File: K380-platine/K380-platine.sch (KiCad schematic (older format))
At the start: 33 parts, among them J1 JST-PH 2, J2 Conn_01x23, J3 MicroMod-M.2E, J4 USB_C_Receptacle_USB2.0, Q1 PMost Enc FET -20V, Q2 Q_NMOS_DGS, SW1 EG1215AA, SW2 SW_Push, SW3 SW_Push, U1 XC6220B331MR, U2 MCP73831-2-OT

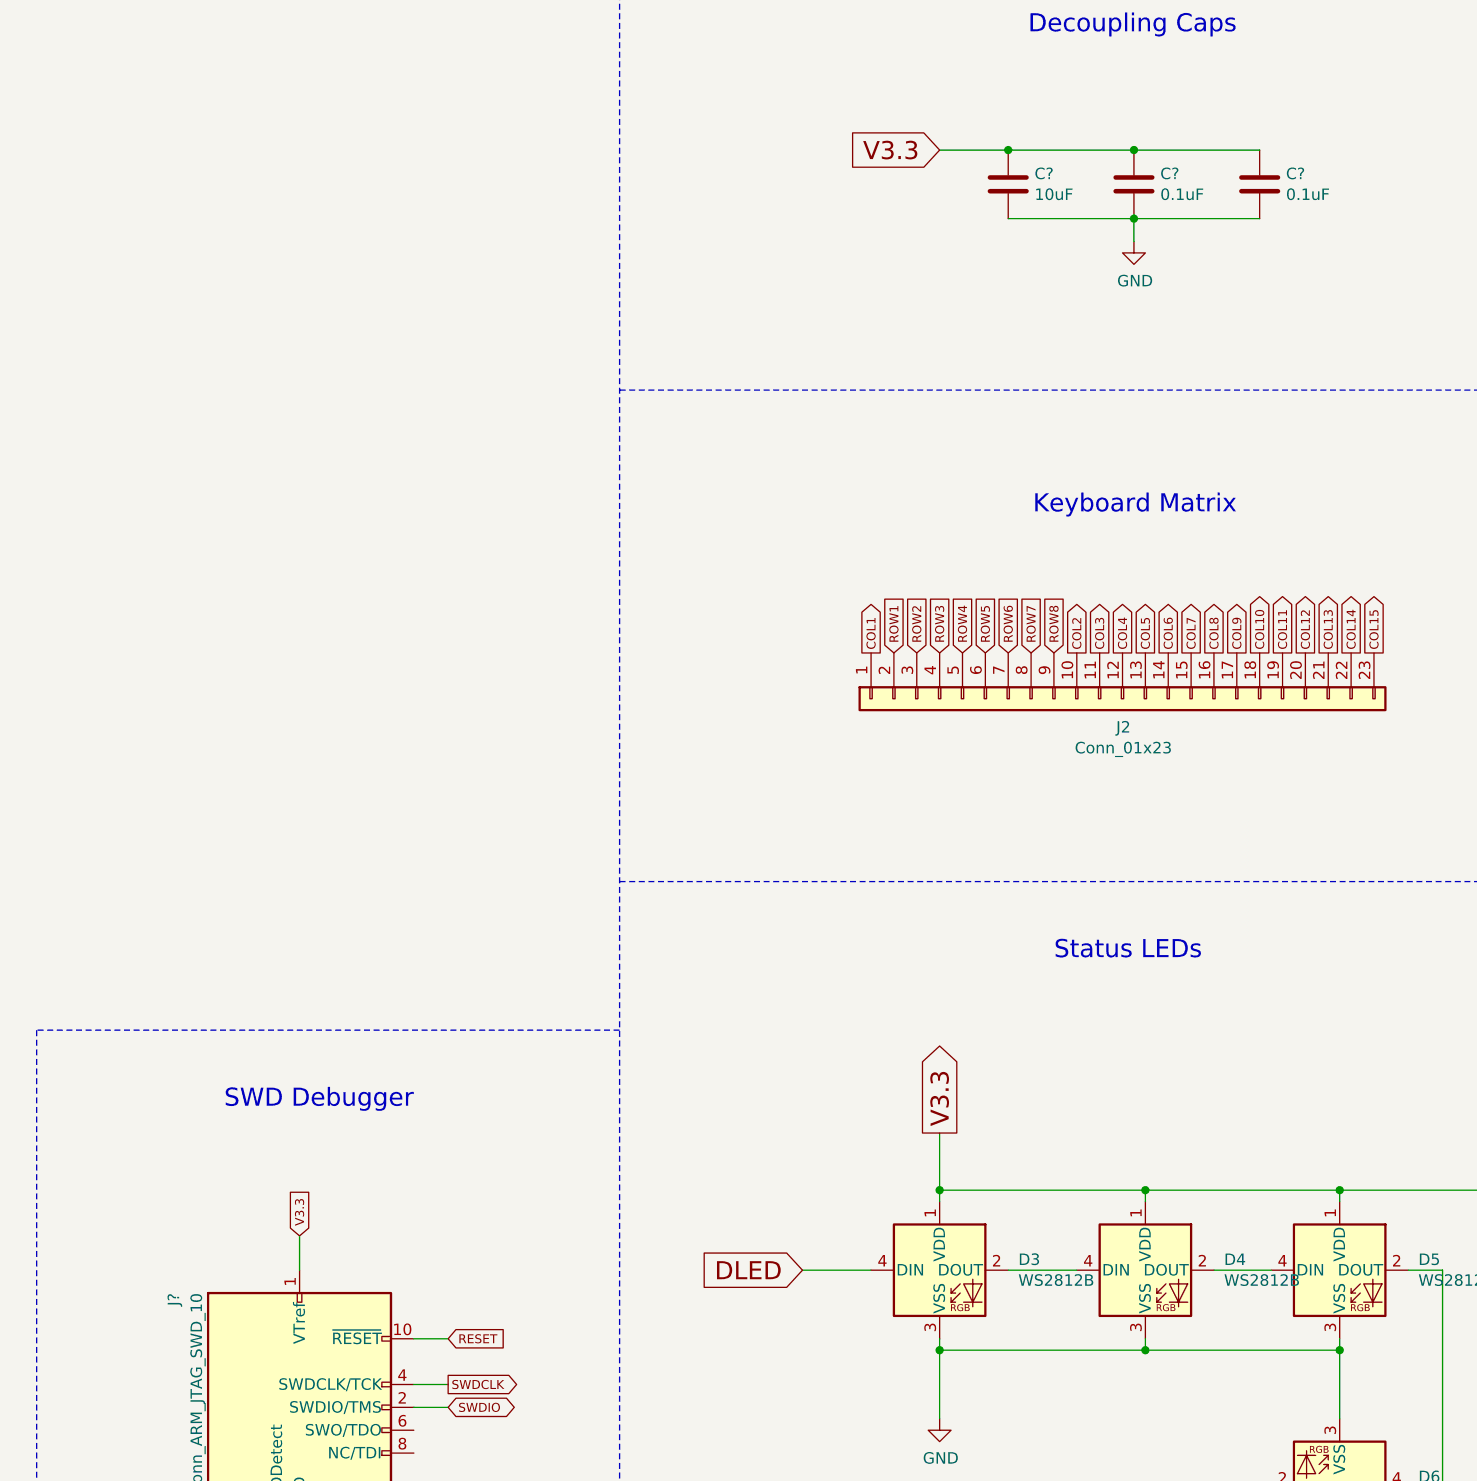
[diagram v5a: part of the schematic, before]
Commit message: Assigned footprint to all components
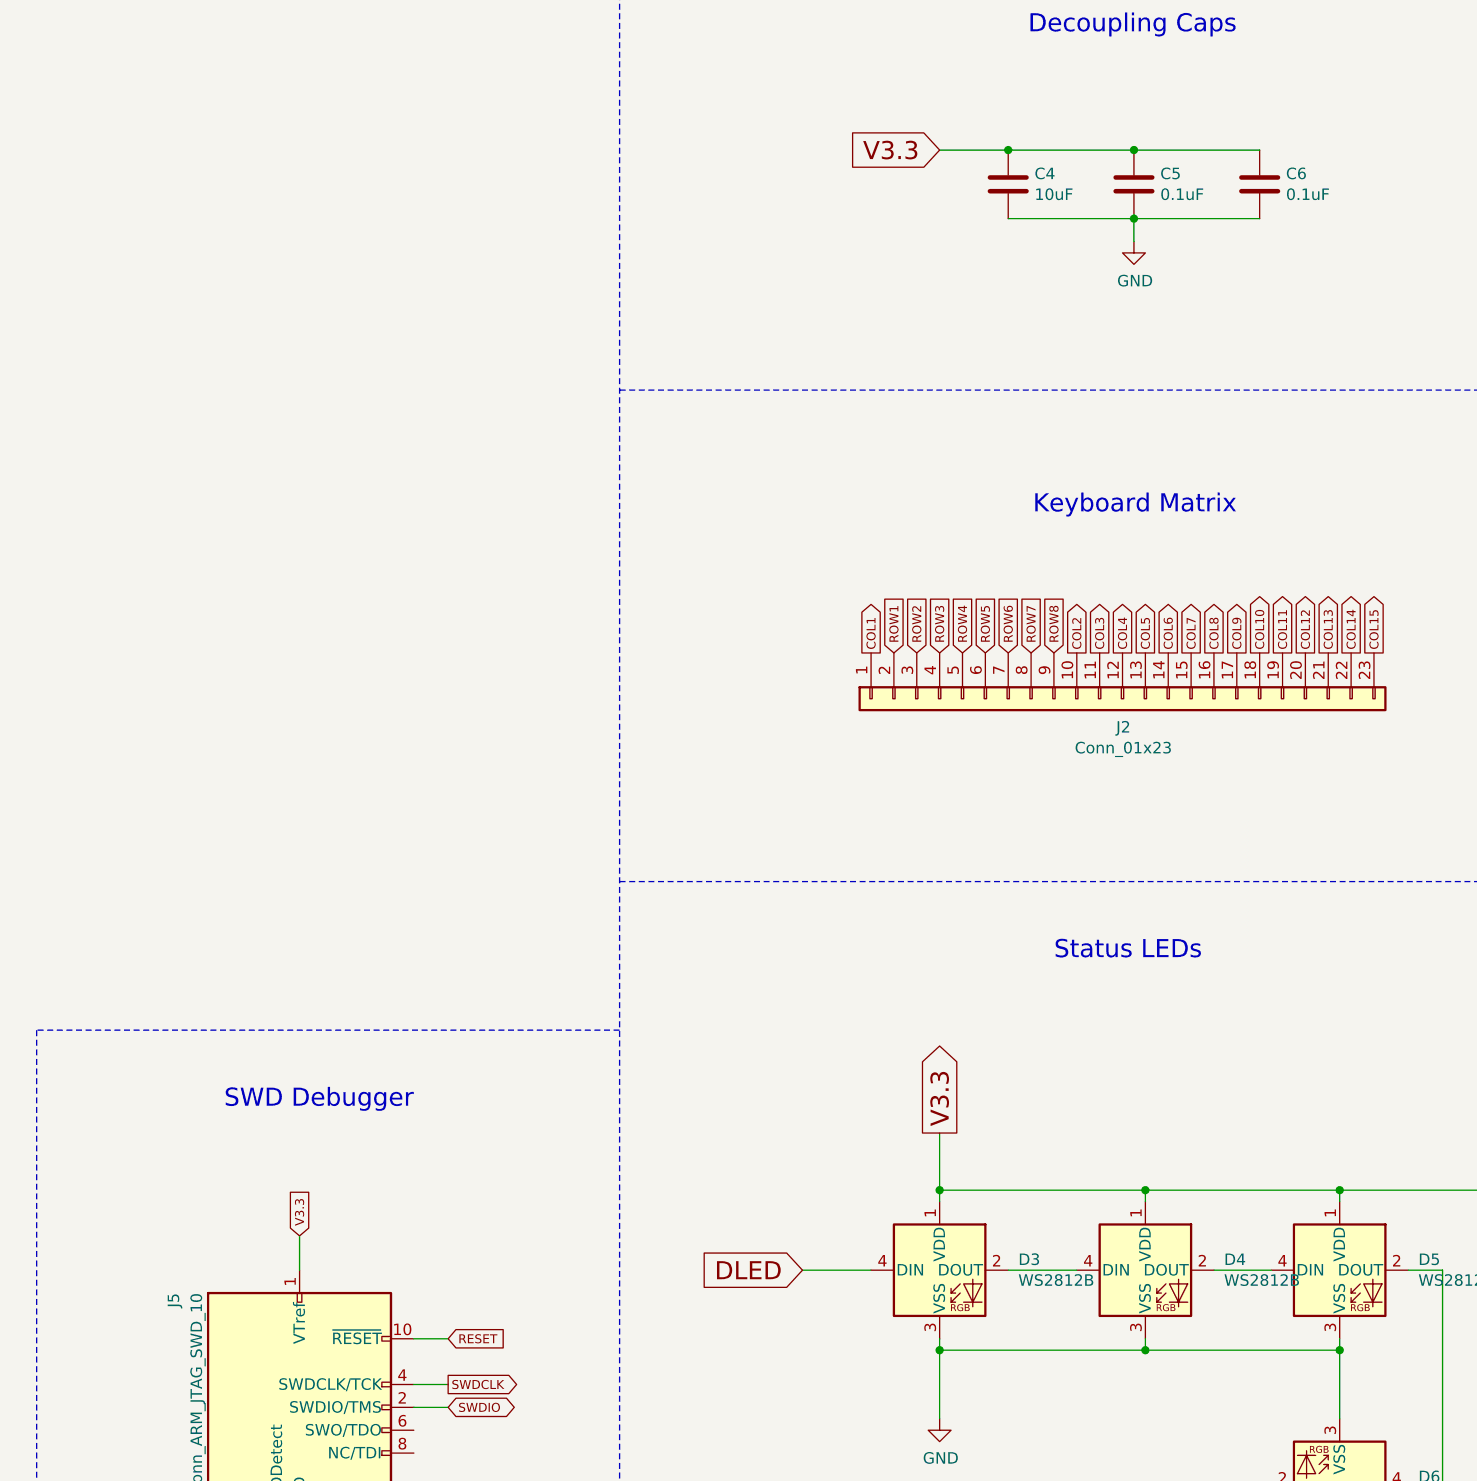
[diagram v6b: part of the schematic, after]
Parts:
- C1, C2, C3: footprint (none) -> Capacitor_SMD:C_1206_3216Metric_Pad1.33x1.80mm_HandSolder
- C4, C5, C6: renamed from C?; footprint (none) -> Capacitor_SMD:C_1206_3216Metric_Pad1.33x1.80mm_HandSolder
- D2: footprint (none) -> Diode_SMD:D_SMA_Handsoldering
- J4, R1, R2, R3, R4, R5, R6, R7, R8, R9: footprint (none) -> Resistor_SMD:R_1206_3216Metric_Pad1.30x1.75mm_HandSolder
- J5: renamed from J?; footprint (none) -> Connector_PinHeader_1.27mm:PinHeader_2x05_P1.27mm_Vertical_SMD
- Q2: footprint (none) -> Package_TO_SOT_SMD:SOT-23
- SW2, SW3: footprint (none) -> LibraryLoader:MJTP1140AAUTR
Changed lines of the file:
@@
 F 0 "C1" H 1742 10446 50  0000 L CNN
 F 1 "10uF" H 1742 10355 50  0000 L CNN
-F 2 "" H 1650 10400 50  0001 C CNN
+F 2 "Capacitor_SMD:C_1206_3216Metric_Pad1.33x1.80mm_HandSolder" H 1650 10400 50  0001 C CNN
 F 3 "~" H 1650 10400 50  0001 C CNN
 	1    1650 10400
@@
 F 0 "R1" H 1209 10446 50  0000 L CNN
 F 1 "100K" H 1209 10355 50  0000 L CNN
-F 2 "" H 1150 10400 50  0001 C CNN
+F 2 "Resistor_SMD:R_1206_3216Metric_Pad1.30x1.75mm_HandSolder" H 1150 10400 50  0001 C CNN
 F 3 "~" H 1150 10400 50  0001 C CNN
 	1    1150 10400
@@
 F 0 "R2" V 1904 10250 50  0000 C CNN
 F 1 "100K" V 1995 10250 50  0000 C CNN
-F 2 "" H 2100 10250 50  0001 C CNN
+F 2 "Resistor_SMD:R_1206_3216Metric_Pad1.30x1.75mm_HandSolder" H 2100 10250 50  0001 C CNN
 F 3 "~" H 2100 10250 50  0001 C CNN
 	1    2100 10250
@@
 F 0 "C2" H 3492 10446 50  0000 L CNN
 F 1 "4.7uF" H 3492 10355 50  0000 L CNN
-F 2 "" H 3400 10400 50  0001 C CNN
+F 2 "Capacitor_SMD:C_1206_3216Metric_Pad1.33x1.80mm_HandSolder" H 3400 10400 50  0001 C CNN
 F 3 "~" H 3400 10400 50  0001 C CNN
 	1    3400 10400
@@
 F 0 "R3" H 5609 9996 50  0000 L CNN
 F 1 "RProg" H 5609 9905 50  0000 L CNN
-F 2 "" H 5550 9950 50  0001 C CNN
+F 2 "Resistor_SMD:R_1206_3216Metric_Pad1.30x1.75mm_HandSolder" H 5550 9950 50  0001 C CNN
 F 3 "~" H 5550 9950 50  0001 C CNN
 	1    5550 9950
@@
 F 0 "C3" H 6992 9896 50  0000 L CNN
 F 1 "10uF" H 6992 9805 50  0000 L CNN
-F 2 "" H 6900 9850 50  0001 C CNN
+F 2 "Capacitor_SMD:C_1206_3216Metric_Pad1.33x1.80mm_HandSolder" H 6900 9850 50  0001 C CNN
 F 3 "~" H 6900 9850 50  0001 C CNN
 	1    6900 9850
@@
 F 0 "J4" H 8757 10617 50  0000 C CNN
 F 1 "USB_C_Receptacle_USB2.0" H 8757 10526 50  0000 C CNN
-F 2 "" H 8800 9750 50  0001 C CNN
+F 2 "Resistor_SMD:R_1206_3216Metric_Pad1.30x1.75mm_HandSolder" H 8800 9750 50  0001 C CNN
 F 3 "https://www.usb.org/sites/default/files/documents/usb_type-c.zip" H 8800 9750 50  0001 C CNN
 	1    8650 9750
@@
 F 0 "D2" V 9304 9030 50  0000 L CNN
 F 1 "TVS 5V" V 9395 9030 50  0000 L CNN
-F 2 "" H 9350 8950 50  0001 C CNN
+F 2 "Diode_SMD:D_SMA_Handsoldering" H 9350 8950 50  0001 C CNN
 F 3 "~" H 9350 8950 50  0001 C CNN
 	1    9350 8950
@@
 F 0 "R4" V 8293 10700 50  0000 C CNN
 F 1 "1M" V 8384 10700 50  0000 C CNN
-F 2 "" V 8430 10700 50  0001 C CNN
+F 2 "Resistor_SMD:R_1206_3216Metric_Pad1.30x1.75mm_HandSolder" V 8430 10700 50  0001 C CNN
 F 3 "~" H 8500 10700 50  0001 C CNN
 	1    8500 10700
@@
 F 0 "R5" V 9643 9350 50  0000 C CNN
 F 1 "5.1k 20%" V 9734 9350 50  0000 C CNN
-F 2 "" V 9780 9350 50  0001 C CNN
+F 2 "Resistor_SMD:R_1206_3216Metric_Pad1.30x1.75mm_HandSolder" V 9780 9350 50  0001 C CNN
 F 3 "~" H 9850 9350 50  0001 C CNN
 	1    9850 9350
@@
 F 0 "R6" V 10050 9450 50  0000 C CNN
 F 1 "5.1k 20%" V 9950 9450 50  0000 C CNN
-F 2 "" V 9780 9450 50  0001 C CNN
+F 2 "Resistor_SMD:R_1206_3216Metric_Pad1.30x1.75mm_HandSolder" V 9780 9450 50  0001 C CNN
 F 3 "~" H 9850 9450 50  0001 C CNN
 	1    9850 9450
@@
 F 0 "Q2" H 1955 9104 50  0000 L CNN
 F 1 "Q_NMOS_DGS" H 1955 9195 50  0000 L CNN
-F 2 "" H 1950 9250 50  0001 C CNN
+F 2 "Package_TO_SOT_SMD:SOT-23" H 1950 9250 50  0001 C CNN
 F 3 "~" H 1750 9150 50  0001 C CNN
 	1    1750 9150
@@
 F 0 "R7" V 2050 9200 50  0000 C CNN
 F 1 "100K" V 2266 9150 50  0000 C CNN
-F 2 "" V 2080 9150 50  0001 C CNN
+F 2 "Resistor_SMD:R_1206_3216Metric_Pad1.30x1.75mm_HandSolder" V 2080 9150 50  0001 C CNN
 F 3 "~" H 2150 9150 50  0001 C CNN
 	1    2150 9150
@@
 F 0 "R8" H 12109 9446 50  0000 L CNN
 F 1 "100K" H 12109 9355 50  0000 L CNN
-F 2 "" H 12050 9400 50  0001 C CNN
+F 2 "Resistor_SMD:R_1206_3216Metric_Pad1.30x1.75mm_HandSolder" H 12050 9400 50  0001 C CNN
 F 3 "~" H 12050 9400 50  0001 C CNN
 	1    12050 9400
@@
 F 0 "R9" H 12109 9846 50  0000 L CNN
 F 1 "100K" H 12109 9755 50  0000 L CNN
-F 2 "" H 12050 9800 50  0001 C CNN
+F 2 "Resistor_SMD:R_1206_3216Metric_Pad1.30x1.75mm_HandSolder" H 12050 9800 50  0001 C CNN
 F 3 "~" H 12050 9800 50  0001 C CNN
 	1    12050 9800
@@
 F 0 "SW2" H 14300 9485 50  0000 C CNN
 F 1 "SW_Push" H 14300 9394 50  0000 C CNN
-F 2 "" H 14300 9400 50  0001 C CNN
+F 2 "LibraryLoader:MJTP1140AAUTR" H 14300 9400 50  0001 C CNN
 F 3 "~" H 14300 9400 50  0001 C CNN
 	1    14300 9200
@@
 F 0 "SW3" H 14300 10335 50  0000 C CNN
 F 1 "SW_Push" H 14300 10244 50  0000 C CNN
-F 2 "" H 14300 10250 50  0001 C CNN
+F 2 "LibraryLoader:MJTP1140AAUTR" H 14300 10250 50  0001 C CNN
 F 3 "~" H 14300 10250 50  0001 C CNN
 	1    14300 10050
@@
 V3.3
 $Comp
-L Device:C C?
+L Device:C C4
 U 1 1 62A35720
 P 13300 1500
-F 0 "C?" H 13415 1546 50  0000 L CNN
+F 0 "C4" H 13415 1546 50  0000 L CNN
 F 1 "10uF" H 13415 1455 50  0000 L CNN
-F 2 "" H 13338 1350 50  0001 C CNN
+F 2 "Capacitor_SMD:C_1206_3216Metric_Pad1.33x1.80mm_HandSolder" H 13338 1350 50  0001 C CNN
 F 3 "~" H 13300 1500 50  0001 C CNN
 	1    13300 1500
@@
 $EndComp
 $Comp
-L Device:C C?
+L Device:C C5
 U 1 1 62A35CBD
 P 13850 1500
-F 0 "C?" H 13965 1546 50  0000 L CNN
+F 0 "C5" H 13965 1546 50  0000 L CNN
 F 1 "0.1uF" H 13965 1455 50  0000 L CNN
-F 2 "" H 13888 1350 50  0001 C CNN
+F 2 "Capacitor_SMD:C_1206_3216Metric_Pad1.33x1.80mm_HandSolder" H 13888 1350 50  0001 C CNN
 F 3 "~" H 13850 1500 50  0001 C CNN
 	1    13850 1500
@@
 $EndComp
 $Comp
-L Device:C C?
+L Device:C C6
 U 1 1 62A35E6F
 P 14400 1500
-F 0 "C?" H 14515 1546 50  0000 L CNN
+F 0 "C6" H 14515 1546 50  0000 L CNN
 F 1 "0.1uF" H 14515 1455 50  0000 L CNN
-F 2 "" H 14438 1350 50  0001 C CNN
+F 2 "Capacitor_SMD:C_1206_3216Metric_Pad1.33x1.80mm_HandSolder" H 14438 1350 50  0001 C CNN
 F 3 "~" H 14400 1500 50  0001 C CNN
 	1    14400 1500
@@
 	13850 1650 14400 1650
 $Comp
-L power:GND #PWR?
+L power:GND #PWR013
 U 1 1 62A3EF82
 P 13850 1750
-F 0 "#PWR?" H 13850 1500 50  0001 C CNN
+F 0 "#PWR013" H 13850 1500 50  0001 C CNN
 F 1 "GND" H 13855 1577 50  0000 C CNN
 F 2 "" H 13850 1750 50  0001 C CNN
@@
 	4200 2750 4400 2750
 $Comp
-L Connector:Conn_ARM_JTAG_SWD_10 J?
+L Connector:Conn_ARM_JTAG_SWD_10 J5
 U 1 1 62AB1718
 P 10200 6850
-F 0 "J?" V 9650 7350 50  0000 R CNN
+F 0 "J5" V 9650 7350 50  0000 R CNN
 F 1 "Conn_ARM_JTAG_SWD_10" V 9750 7350 50  0000 R CNN
-F 2 "" H 10200 6850 50  0001 C CNN
+F 2 "Connector_PinHeader_1.27mm:PinHeader_2x05_P1.27mm_Vertical_SMD" H 10200 6850 50  0001 C CNN
 F 3 "http://infocenter.arm.com/help/topic/com.arm.doc.ddi0314h/DDI0314H_coresight_components_trm.pdf" V 9850 5600 50  0001 C CNN
 	1    10200 6850
@@
 SWDCLK
 $Comp
-L power:GND #PWR?
+L power:GND #PWR012
 U 1 1 62AB49D1
 P 10200 7550
-F 0 "#PWR?" H 10200 7300 50  0001 C CNN
+F 0 "#PWR012" H 10200 7300 50  0001 C CNN
 F 1 "GND" H 10205 7377 50  0000 C CNN
 F 2 "" H 10200 7550 50  0001 C CNN
@@
 	5800 4850 5600 4850
 $Comp
-L power:GND #PWR?
+L power:GND #PWR011
 U 1 1 62B9D125
 P 5000 5600
-F 0 "#PWR?" H 5000 5350 50  0001 C CNN
+F 0 "#PWR011" H 5000 5350 50  0001 C CNN
 F 1 "GND" H 5005 5427 50  0000 C CNN
 F 2 "" H 5000 5600 50  0001 C CNN

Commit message: Fix footprint of USB-c connector
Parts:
- C1, C2, C3, C4, C5, C6: footprint Capacitor_SMD:C_1206_3216Metric_Pad1.33x1.80mm_HandSolder -> Capacitor_SMD:C_0805_2012Metric_Pad1.18x1.45mm_HandSolder
- J4: footprint Resistor_SMD:R_1206_3216Metric_Pad1.30x1.75mm_HandSolder -> Connector_USB:USB_C_Receptacle_GCT_USB4085
- R1, R2, R4, R5, R6, R7, R8, R9: footprint Resistor_SMD:R_1206_3216Metric_Pad1.30x1.75mm_HandSolder -> Resistor_SMD:R_0805_2012Metric_Pad1.20x1.40mm_HandSolder
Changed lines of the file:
@@
 F 0 "C1" H 1742 10446 50  0000 L CNN
 F 1 "10uF" H 1742 10355 50  0000 L CNN
-F 2 "Capacitor_SMD:C_1206_3216Metric_Pad1.33x1.80mm_HandSolder" H 1650 10400 50  0001 C CNN
+F 2 "Capacitor_SMD:C_0805_2012Metric_Pad1.18x1.45mm_HandSolder" H 1650 10400 50  0001 C CNN
 F 3 "~" H 1650 10400 50  0001 C CNN
 	1    1650 10400
@@
 F 0 "R1" H 1209 10446 50  0000 L CNN
 F 1 "100K" H 1209 10355 50  0000 L CNN
-F 2 "Resistor_SMD:R_1206_3216Metric_Pad1.30x1.75mm_HandSolder" H 1150 10400 50  0001 C CNN
+F 2 "Resistor_SMD:R_0805_2012Metric_Pad1.20x1.40mm_HandSolder" H 1150 10400 50  0001 C CNN
 F 3 "~" H 1150 10400 50  0001 C CNN
 	1    1150 10400
@@
 F 0 "R2" V 1904 10250 50  0000 C CNN
 F 1 "100K" V 1995 10250 50  0000 C CNN
-F 2 "Resistor_SMD:R_1206_3216Metric_Pad1.30x1.75mm_HandSolder" H 2100 10250 50  0001 C CNN
+F 2 "Resistor_SMD:R_0805_2012Metric_Pad1.20x1.40mm_HandSolder" H 2100 10250 50  0001 C CNN
 F 3 "~" H 2100 10250 50  0001 C CNN
 	1    2100 10250
@@
 F 0 "C2" H 3492 10446 50  0000 L CNN
 F 1 "4.7uF" H 3492 10355 50  0000 L CNN
-F 2 "Capacitor_SMD:C_1206_3216Metric_Pad1.33x1.80mm_HandSolder" H 3400 10400 50  0001 C CNN
+F 2 "Capacitor_SMD:C_0805_2012Metric_Pad1.18x1.45mm_HandSolder" H 3400 10400 50  0001 C CNN
 F 3 "~" H 3400 10400 50  0001 C CNN
 	1    3400 10400
@@
 F 0 "C3" H 6992 9896 50  0000 L CNN
 F 1 "10uF" H 6992 9805 50  0000 L CNN
-F 2 "Capacitor_SMD:C_1206_3216Metric_Pad1.33x1.80mm_HandSolder" H 6900 9850 50  0001 C CNN
+F 2 "Capacitor_SMD:C_0805_2012Metric_Pad1.18x1.45mm_HandSolder" H 6900 9850 50  0001 C CNN
 F 3 "~" H 6900 9850 50  0001 C CNN
 	1    6900 9850
@@
 F 0 "J4" H 8757 10617 50  0000 C CNN
 F 1 "USB_C_Receptacle_USB2.0" H 8757 10526 50  0000 C CNN
-F 2 "Resistor_SMD:R_1206_3216Metric_Pad1.30x1.75mm_HandSolder" H 8800 9750 50  0001 C CNN
+F 2 "Connector_USB:USB_C_Receptacle_GCT_USB4085" H 8800 9750 50  0001 C CNN
 F 3 "https://www.usb.org/sites/default/files/documents/usb_type-c.zip" H 8800 9750 50  0001 C CNN
 	1    8650 9750
@@
 F 0 "R4" V 8293 10700 50  0000 C CNN
 F 1 "1M" V 8384 10700 50  0000 C CNN
-F 2 "Resistor_SMD:R_1206_3216Metric_Pad1.30x1.75mm_HandSolder" V 8430 10700 50  0001 C CNN
+F 2 "Resistor_SMD:R_0805_2012Metric_Pad1.20x1.40mm_HandSolder" V 8430 10700 50  0001 C CNN
 F 3 "~" H 8500 10700 50  0001 C CNN
 	1    8500 10700
@@
 F 0 "R5" V 9643 9350 50  0000 C CNN
 F 1 "5.1k 20%" V 9734 9350 50  0000 C CNN
-F 2 "Resistor_SMD:R_1206_3216Metric_Pad1.30x1.75mm_HandSolder" V 9780 9350 50  0001 C CNN
+F 2 "Resistor_SMD:R_0805_2012Metric_Pad1.20x1.40mm_HandSolder" V 9780 9350 50  0001 C CNN
 F 3 "~" H 9850 9350 50  0001 C CNN
 	1    9850 9350
@@
 F 0 "R6" V 10050 9450 50  0000 C CNN
 F 1 "5.1k 20%" V 9950 9450 50  0000 C CNN
-F 2 "Resistor_SMD:R_1206_3216Metric_Pad1.30x1.75mm_HandSolder" V 9780 9450 50  0001 C CNN
+F 2 "Resistor_SMD:R_0805_2012Metric_Pad1.20x1.40mm_HandSolder" V 9780 9450 50  0001 C CNN
 F 3 "~" H 9850 9450 50  0001 C CNN
 	1    9850 9450
@@
 F 0 "R7" V 2050 9200 50  0000 C CNN
 F 1 "100K" V 2266 9150 50  0000 C CNN
-F 2 "Resistor_SMD:R_1206_3216Metric_Pad1.30x1.75mm_HandSolder" V 2080 9150 50  0001 C CNN
+F 2 "Resistor_SMD:R_0805_2012Metric_Pad1.20x1.40mm_HandSolder" V 2080 9150 50  0001 C CNN
 F 3 "~" H 2150 9150 50  0001 C CNN
 	1    2150 9150
@@
 F 0 "R8" H 12109 9446 50  0000 L CNN
 F 1 "100K" H 12109 9355 50  0000 L CNN
-F 2 "Resistor_SMD:R_1206_3216Metric_Pad1.30x1.75mm_HandSolder" H 12050 9400 50  0001 C CNN
+F 2 "Resistor_SMD:R_0805_2012Metric_Pad1.20x1.40mm_HandSolder" H 12050 9400 50  0001 C CNN
 F 3 "~" H 12050 9400 50  0001 C CNN
 	1    12050 9400
@@
 F 0 "R9" H 12109 9846 50  0000 L CNN
 F 1 "100K" H 12109 9755 50  0000 L CNN
-F 2 "Resistor_SMD:R_1206_3216Metric_Pad1.30x1.75mm_HandSolder" H 12050 9800 50  0001 C CNN
+F 2 "Resistor_SMD:R_0805_2012Metric_Pad1.20x1.40mm_HandSolder" H 12050 9800 50  0001 C CNN
 F 3 "~" H 12050 9800 50  0001 C CNN
 	1    12050 9800
@@
 F 0 "C4" H 13415 1546 50  0000 L CNN
 F 1 "10uF" H 13415 1455 50  0000 L CNN
-F 2 "Capacitor_SMD:C_1206_3216Metric_Pad1.33x1.80mm_HandSolder" H 13338 1350 50  0001 C CNN
+F 2 "Capacitor_SMD:C_0805_2012Metric_Pad1.18x1.45mm_HandSolder" H 13338 1350 50  0001 C CNN
 F 3 "~" H 13300 1500 50  0001 C CNN
 	1    13300 1500
@@
 F 0 "C5" H 13965 1546 50  0000 L CNN
 F 1 "0.1uF" H 13965 1455 50  0000 L CNN
-F 2 "Capacitor_SMD:C_1206_3216Metric_Pad1.33x1.80mm_HandSolder" H 13888 1350 50  0001 C CNN
+F 2 "Capacitor_SMD:C_0805_2012Metric_Pad1.18x1.45mm_HandSolder" H 13888 1350 50  0001 C CNN
 F 3 "~" H 13850 1500 50  0001 C CNN
 	1    13850 1500
@@
 F 0 "C6" H 14515 1546 50  0000 L CNN
 F 1 "0.1uF" H 14515 1455 50  0000 L CNN
-F 2 "Capacitor_SMD:C_1206_3216Metric_Pad1.33x1.80mm_HandSolder" H 14438 1350 50  0001 C CNN
+F 2 "Capacitor_SMD:C_0805_2012Metric_Pad1.18x1.45mm_HandSolder" H 14438 1350 50  0001 C CNN
 F 3 "~" H 14400 1500 50  0001 C CNN
 	1    14400 1500
